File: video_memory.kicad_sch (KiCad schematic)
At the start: 22 parts, among them J11 74LS245, J9 uPD446, K15 7417, U2 74LS10

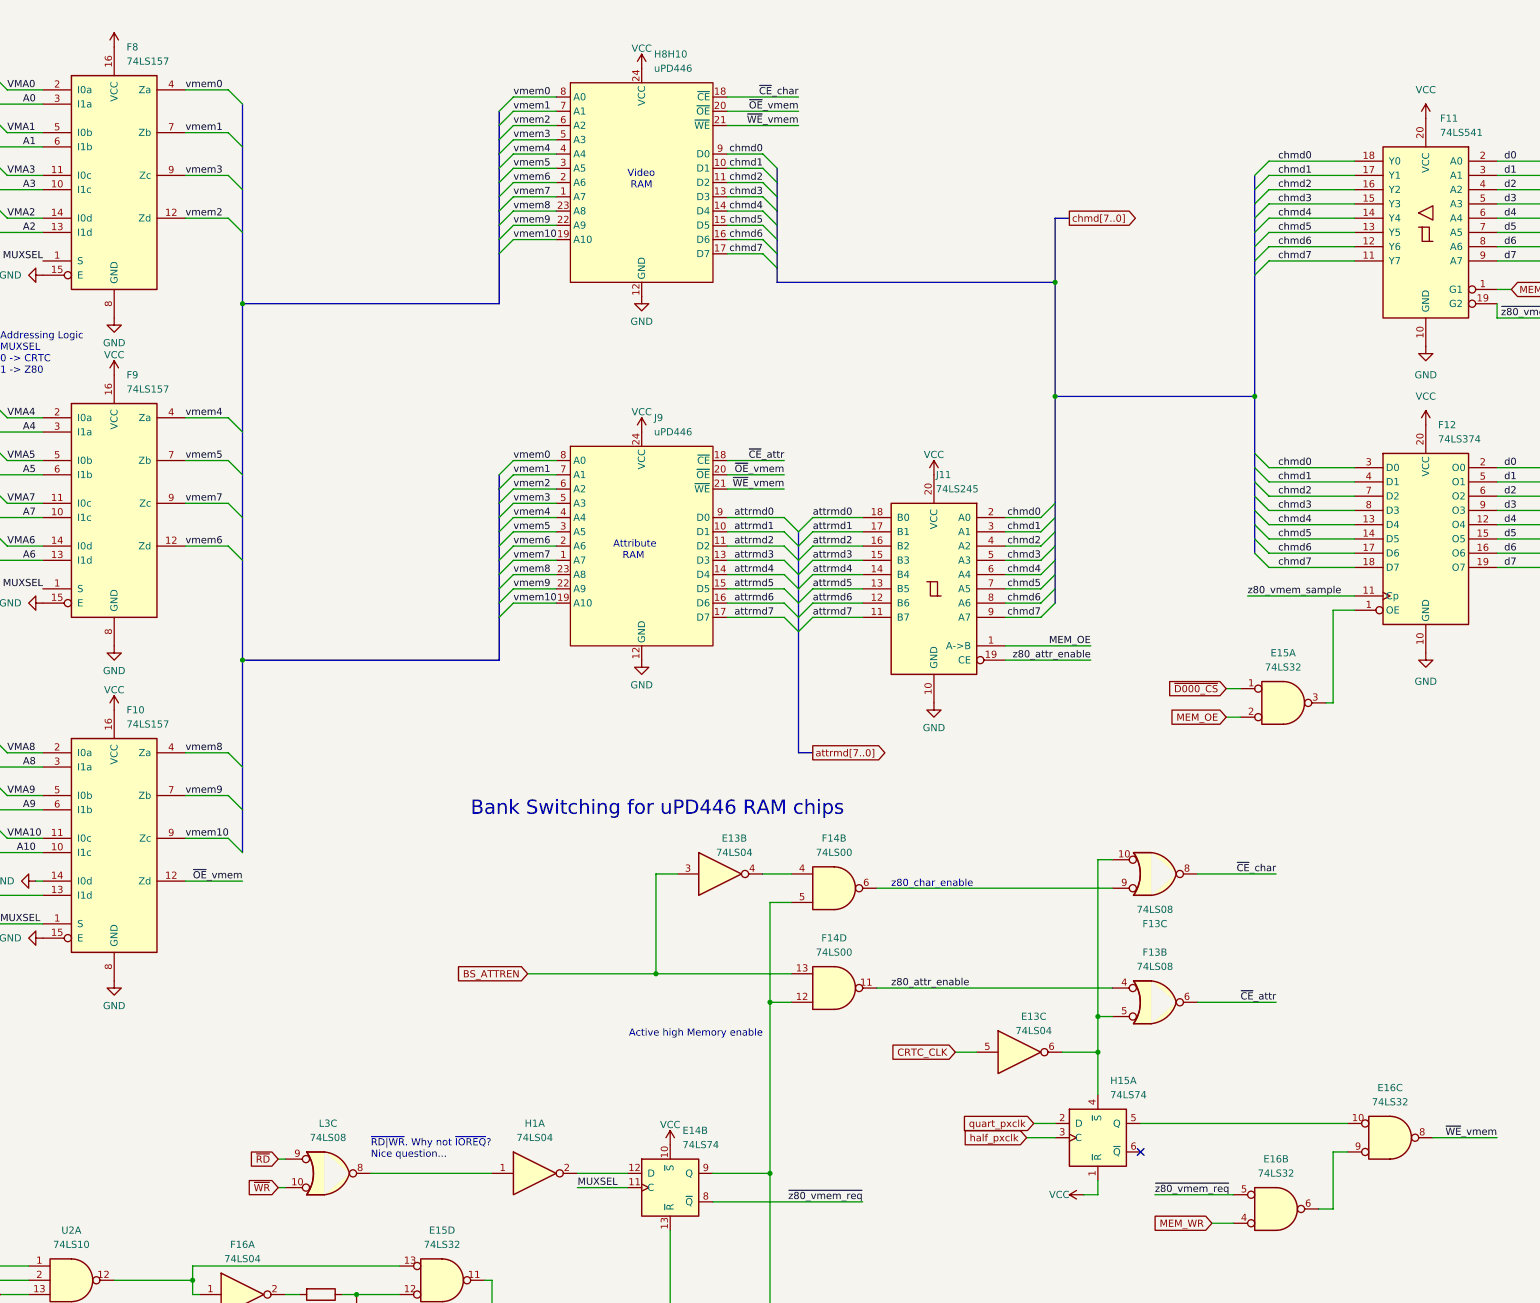
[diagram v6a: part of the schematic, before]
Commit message: VCC -> +5V
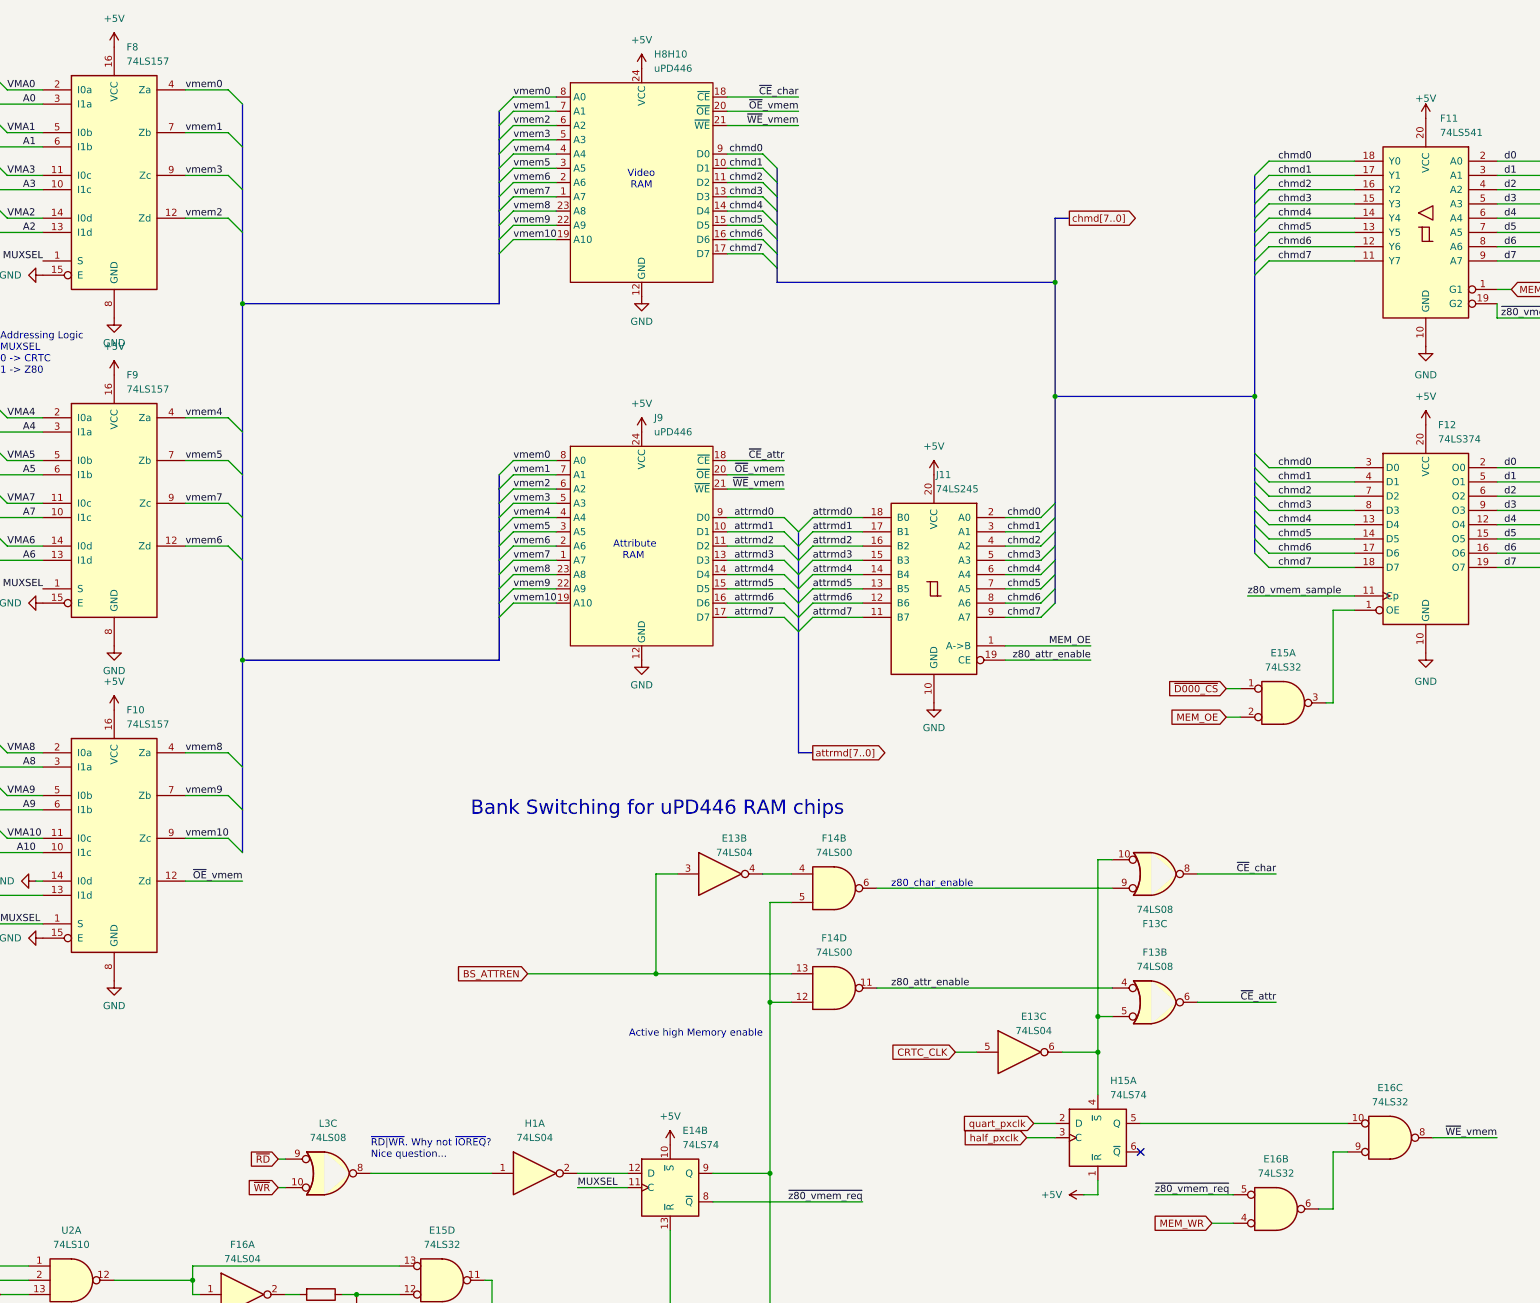
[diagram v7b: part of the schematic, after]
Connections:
- net VCC renamed +5V
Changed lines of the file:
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@@
     )
   )
-  (symbol (lib_name "VCC_1") (lib_id "power:VCC") (at 308.61 85.09 0) (mirror y) (unit 1)
+  (symbol (lib_id "power:+5V") (at 308.61 85.09 0) (mirror y) (unit 1)
     (in_bom yes) (on_board yes) (dnp no) (fields_autoplaced)
     (property "Reference" "#PWR?" (at 308.61 88.9 0)
       (effects (font (size 1.27 1.27)) hide)
     )
-    (property "Value" "VCC" (at 308.61 80.01 0)
+    (property "Value" "+5V" (at 308.61 80.01 0)
       (effects (font (size 1.27 1.27)))
     )
@@
         )
         (path "/12a6dbe3-008d-4c5b-88f6-9f1c816060be/3df68a1a-abd3-4ad7-9eb9-855dfc37a3a7"
-          (reference "#PWR0200") (unit 1)
-        )
-      )
-    )
-  )
-  (symbol (lib_id "power:VCC") (at 74.93 76.2 0) (unit 1)
+          (reference "#PWR?") (unit 1)
+        )
+      )
+    )
+  )
+  (symbol (lib_id "power:+5V") (at 74.93 76.2 0) (unit 1)
     (in_bom yes) (on_board yes) (dnp no) (fields_autoplaced)
     (property "Reference" "#PWR?" (at 74.93 80.01 0)
       (effects (font (size 1.27 1.27)) hide)
     )
-    (property "Value" "VCC" (at 74.93 72.6242 0)
+    (property "Value" "+5V" (at 74.93 71.12 0)
       (effects (font (size 1.27 1.27)))
     )
@@
         )
         (path "/12a6dbe3-008d-4c5b-88f6-9f1c816060be/3df68a1a-abd3-4ad7-9eb9-855dfc37a3a7"
-          (reference "#PWR0189") (unit 1)
+          (reference "#PWR?") (unit 1)
         )
       )
@@
     )
   )
-  (symbol (lib_name "VCC_7") (lib_id "power:VCC") (at 173.99 213.36 0) (unit 1)
+  (symbol (lib_id "power:+5V") (at 173.99 213.36 0) (unit 1)
     (in_bom yes) (on_board yes) (dnp no) (fields_autoplaced)
     (property "Reference" "#PWR049" (at 173.99 217.17 0)
       (effects (font (size 1.27 1.27)) hide)
     )
-    (property "Value" "VCC" (at 173.99 209.7842 0)
+    (property "Value" "+5V" (at 173.99 208.28 0)
       (effects (font (size 1.27 1.27)))
     )
@@
         )
         (path "/12a6dbe3-008d-4c5b-88f6-9f1c816060be/3df68a1a-abd3-4ad7-9eb9-855dfc37a3a7"
-          (reference "#PWR0206") (unit 1)
+          (reference "#PWR?") (unit 1)
         )
       )
@@
     )
   )
-  (symbol (lib_id "power:VCC") (at 168.91 21.59 0) (unit 1)
+  (symbol (lib_id "power:+5V") (at 168.91 21.59 0) (unit 1)
     (in_bom yes) (on_board yes) (dnp no) (fields_autoplaced)
     (property "Reference" "#PWR?" (at 168.91 25.4 0)
       (effects (font (size 1.27 1.27)) hide)
     )
-    (property "Value" "VCC" (at 168.91 18.0142 0)
+    (property "Value" "+5V" (at 168.91 16.51 0)
       (effects (font (size 1.27 1.27)))
     )
@@
         )
         (path "/12a6dbe3-008d-4c5b-88f6-9f1c816060be/3df68a1a-abd3-4ad7-9eb9-855dfc37a3a7"
-          (reference "#PWR0195") (unit 1)
+          (reference "#PWR?") (unit 1)
         )
       )
@@
     )
   )
-  (symbol (lib_name "VCC_12") (lib_id "power:VCC") (at 308.61 30.48 0) (mirror y) (unit 1)
+  (symbol (lib_id "power:+5V") (at 308.61 30.48 0) (mirror y) (unit 1)
     (in_bom yes) (on_board yes) (dnp no)
     (property "Reference" "#PWR?" (at 308.61 34.29 0)
       (effects (font (size 1.27 1.27)) hide)
     )
-    (property "Value" "VCC" (at 308.61 25.4 0)
+    (property "Value" "+5V" (at 308.61 26.924 0)
       (effects (font (size 1.27 1.27)))
     )
@@
         )
         (path "/12a6dbe3-008d-4c5b-88f6-9f1c816060be/3df68a1a-abd3-4ad7-9eb9-855dfc37a3a7"
-          (reference "#PWR0204") (unit 1)
+          (reference "#PWR?") (unit 1)
         )
       )
@@
     )
   )
-  (symbol (lib_name "VCC_2") (lib_id "power:VCC") (at 247.65 222.25 90) (unit 1)
+  (symbol (lib_id "power:+5V") (at 247.65 222.25 90) (unit 1)
     (in_bom yes) (on_board yes) (dnp no) (fields_autoplaced)
     (property "Reference" "#PWR0115" (at 251.46 222.25 0)
       (effects (font (size 1.27 1.27)) hide)
     )
-    (property "Value" "VCC" (at 245.11 222.25 90)
+    (property "Value" "+5V" (at 243.84 222.25 90)
       (effects (font (size 1.27 1.27)) (justify left))
     )
@@
         )
         (path "/12a6dbe3-008d-4c5b-88f6-9f1c816060be/3df68a1a-abd3-4ad7-9eb9-855dfc37a3a7"
-          (reference "#PWR0202") (unit 1)
+          (reference "#PWR?") (unit 1)
         )
       )
@@
     )
   )
-  (symbol (lib_name "VCC_5") (lib_id "power:VCC") (at 220.98 93.98 0) (unit 1)
+  (symbol (lib_id "power:+5V") (at 220.98 93.98 0) (unit 1)
     (in_bom yes) (on_board yes) (dnp no) (fields_autoplaced)
     (property "Reference" "#PWR?" (at 220.98 97.79 0)
       (effects (font (size 1.27 1.27)) hide)
     )
-    (property "Value" "VCC" (at 220.98 90.4042 0)
+    (property "Value" "+5V" (at 220.98 88.9 0)
       (effects (font (size 1.27 1.27)))
     )
@@
         )
         (path "/12a6dbe3-008d-4c5b-88f6-9f1c816060be/3df68a1a-abd3-4ad7-9eb9-855dfc37a3a7"
-          (reference "#PWR0198") (unit 1)
+          (reference "#PWR?") (unit 1)
         )
       )
@@
     )
   )
-  (symbol (lib_id "power:VCC") (at 74.93 17.78 0) (unit 1)
+  (symbol (lib_id "power:+5V") (at 74.93 17.78 0) (unit 1)
     (in_bom yes) (on_board yes) (dnp no) (fields_autoplaced)
     (property "Reference" "#PWR?" (at 74.93 21.59 0)
       (effects (font (size 1.27 1.27)) hide)
     )
-    (property "Value" "VCC" (at 74.93 14.2042 0)
-      (effects (font (size 1.27 1.27)) hide)
+    (property "Value" "+5V" (at 74.93 12.7 0)
+      (effects (font (size 1.27 1.27)))
     )
     (property "Footprint" "" (at 74.93 17.78 0)
@@
         )
         (path "/12a6dbe3-008d-4c5b-88f6-9f1c816060be/3df68a1a-abd3-4ad7-9eb9-855dfc37a3a7"
-          (reference "#PWR0192") (unit 1)
+          (reference "#PWR?") (unit 1)
         )
       )
@@
     )
   )
-  (symbol (lib_name "VCC_4") (lib_id "power:VCC") (at 168.91 86.36 0) (unit 1)
+  (symbol (lib_id "power:+5V") (at 168.91 86.36 0) (unit 1)
     (in_bom yes) (on_board yes) (dnp no) (fields_autoplaced)
     (property "Reference" "#PWR?" (at 168.91 90.17 0)
       (effects (font (size 1.27 1.27)) hide)
     )
-    (property "Value" "VCC" (at 168.91 82.7842 0)
+    (property "Value" "+5V" (at 168.91 81.28 0)
       (effects (font (size 1.27 1.27)))
     )
@@
         )
         (path "/12a6dbe3-008d-4c5b-88f6-9f1c816060be/3df68a1a-abd3-4ad7-9eb9-855dfc37a3a7"
-          (reference "#PWR0199") (unit 1)
+          (reference "#PWR?") (unit 1)
         )
       )
@@
     )
   )
-  (symbol (lib_id "power:VCC") (at 74.93 135.89 0) (unit 1)
+  (symbol (lib_id "power:+5V") (at 74.93 135.89 0) (unit 1)
     (in_bom yes) (on_board yes) (dnp no) (fields_autoplaced)
     (property "Reference" "#PWR?" (at 74.93 139.7 0)
       (effects (font (size 1.27 1.27)) hide)
     )
-    (property "Value" "VCC" (at 74.93 132.3142 0)
+    (property "Value" "+5V" (at 74.93 130.81 0)
       (effects (font (size 1.27 1.27)))
     )
@@
         )
         (path "/12a6dbe3-008d-4c5b-88f6-9f1c816060be/3df68a1a-abd3-4ad7-9eb9-855dfc37a3a7"
-          (reference "#PWR0188") (unit 1)
-        )
-      )
+          (reference "#PWR?") (unit 1)
+        )
+      )
